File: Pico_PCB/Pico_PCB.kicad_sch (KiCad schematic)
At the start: 14 parts, among them J1 USB_A, J2 AVR-ISP-6, SW1 SPST_Momentary_4.6x2.8mm, U1 AT90USB647-A

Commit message: PCB_19/09
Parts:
- removed C1, C2, C4: C, symbol Device:C
- removed J2: AVR-ISP-6, symbol Connector:AVR-ISP-6
- removed L1: L, symbol Device:L
- added C10, C11: 100nF, Capacitor_SMD:C_0603_1608Metric_Pad1.08x0.95mm_HandSolder, symbol Device:C
- added C7, C8: 22 pF, Capacitor_SMD:C_0603_1608Metric_Pad1.08x0.95mm_HandSolder, symbol Device:C
- added C9: 4.7uF, Capacitor_SMD:C_0603_1608Metric_Pad1.08x0.95mm_HandSolder, symbol Device:C
- added D10, D11, D3, D4, D5, D6, D7, D8, D9: LED, LED_SMD:LED_0603_1608Metric_Pad1.05x0.95mm_HandSolder, symbol Device:LED
- added J4: Conn_02x04_Counter_Clockwise, Connector_IDC:IDC-Header_2x04_P2.54mm_Vertical, symbol Connector_Generic:Conn_02x04_Counter_Clockwise
- added R10, R11, R12, R13, R14, R5, R6, R8, R9: 1k, symbol Device:R
- added R4: 10k, symbol Device:R
- added R7: 1M, symbol Device:R
- added SW2: SPST_Momentary_4.6x2.8mm, SparkFun-Switch:Momentary_SMD_4.6x2.8mm, symbol SparkFun-Switch:SPST_Momentary_4.6x2.8mm
- added TP1, TP10, TP11, TP12, TP13, TP14, TP15, TP16, TP17, TP18, TP19, TP2, TP20, TP21, TP22, TP23, TP24, TP25, TP26, TP27, TP28, TP29, TP3, TP30, TP31, TP32, TP33, TP34, TP4, TP5, TP6, TP7, TP8, TP9: TestPoint, symbol Connector:TestPoint
- added Y1: Crystal_GND24, Crystal:Crystal_SMD_SeikoEpson_FA238-4Pin_3.2x2.5mm_HandSoldering, symbol Device:Crystal_GND24
- C3: value C -> 1uF
- R1, R2: value R -> 22
- R3: value R -> 10k
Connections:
- net 5V is gone; now on net +5V: J1.1 (VBUS), R3.1, U1.21 (VCC), U1.3 (UVCC), U1.52 (VCC), U1.64 (AVCC)
- net D+: now also R2.1; no longer R2.2
- net D-: now also R1.1; no longer R1.2
- net GND: now also D1.2 (A), D2.2 (A), C10.2, C11.2, C7.2, C8.2, C9.2, D10.1 (K), D11.1 (K), D3.1 (K), D4.1 (K), D5.1 (K), D6.1 (K), D7.1 (K), D8.1 (K), D9.1 (K), J4.1 (Pin_1), SW2.1 (A), Y1.2, Y1.4
- net MISO: now also J4.5 (Pin_5)
- net MOSI: now also J4.3 (Pin_3)
- net RESET: now also J4.6 (Pin_6)
- net SCK: now also J4.7 (Pin_7)
- net SS: now also J4.8 (Pin_8)
- net at D2.1 (K), J1.2 (D-): now also R1.2; no longer R1.1
- net at D1.1 (K), J1.3 (D+): now also R2.2; no longer R2.1
- net at U1.1 (PE6): now also TP27.1
- net INT: now reaches U1.14 (PB4)
- net INT: now also J4.4 (Pin_4)
- net at U1.15 (PB5): now also TP9.1
- net at U1.16 (PB6): now also TP10.1
- net at U1.17 (PB7): now also TP11.1
- net at U1.18 (PE4): now also TP25.1
- net at U1.19 (PE5): now also TP26.1
- net at U1.2 (PE7): now also TP28.1
- net at U1.23 (XTAL2): now also C8.1, R7.2, Y1.3
- net at U1.24 (XTAL1): now also C7.1, R7.1, Y1.1
- net at U1.25 (PD0): now also TP12.1
- net at U1.26 (PD1): now also TP13.1
- net at U1.27 (PD2): now also TP14.1
- net at U1.28 (PD3): now also TP15.1
- net at U1.29 (PD4): now also TP16.1
- net at U1.30 (PD5): now also TP17.1
- net at U1.31 (PD6): now also TP18.1
- net at U1.32 (PD7): now also TP19.1
- net at U1.33 (PE0): now also TP23.1
- net TEST0: now reaches U1.35 (PC0)
- net TEST0: now also R5.1
- net TEST1: now reaches U1.36 (PC1)
- net TEST1: now also R8.1
- net TEST2: now reaches U1.37 (PC2)
- net TEST2: now also R9.1
- net TEST3: now reaches U1.38 (PC3)
- net TEST3: now also R10.1
- net TEST4: now reaches U1.39 (PC4)
- net TEST4: now also R11.1
- net TEST5: now reaches U1.40 (PC5)
- net TEST5: now also R12.1
- net TEST6: now reaches U1.41 (PC6)
- net TEST6: now also R13.1
- net TEST7: now reaches U1.42 (PC7)
- net TEST7: now also R14.1
- net HWB: now reaches U1.43 (PE2/~{HWB})
- net HWB: now also R4.2, SW2.2 (B)
- net at U1.44 (PA7): now also TP8.1
- net at U1.45 (PA6): now also TP7.1
- net at U1.46 (PA5): now also TP6.1
- net at U1.47 (PA4): now also TP5.1
- net at U1.48 (PA3): now also TP4.1
- net at U1.49 (PA2): now also TP3.1
- net at U1.50 (PA1): now also TP2.1
- net at U1.51 (PA0): now also TP1.1
- net at U1.54 (PF7): now also TP20.1
- net at U1.55 (PF6): now also TP21.1
- net at U1.56 (PF5): now also TP34.1
- net at U1.57 (PF4): now also TP33.1
- net at U1.58 (PF3): now also TP32.1
- net at U1.59 (PF2): now also TP31.1
- net at U1.60 (PF1): now also TP30.1
- net at U1.61 (PF0): now also TP29.1
- net at U1.62 (AREF): now also TP22.1
- net +5V: now reaches U1.8 (VBUS)
- net +5V: now also C10.1, C11.1, C9.1, J4.2 (Pin_2), R4.1, R6.1
- net at U1.9 (PE3): now also TP24.1
- new net: D10.2 (A), R13.2
- new net: D11.2 (A), R14.2
- new net: D3.2 (A), R5.2
- new net: D8.2 (A), R11.2
- new net: D7.2 (A), R10.2
- new net: D4.2 (A), R8.2
- new net: D9.2 (A), R12.2
- new net: D5.2 (A), R6.2
- new net: D6.2 (A), R9.2
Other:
- note added: "Bouton HWB"
- note added: "Bouton de reset"
- note added: "Connection HE10"
- note added: "Découplage"
- note added: "LEDs de test"
- note added: "Port USB"
- moved on the sheet: C3, D1, D2, J1, R1, R2, R3, SW1, U1

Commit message: Routage_22_09
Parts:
- C3: footprint (none) -> Capacitor_SMD:C_0603_1608Metric_Pad1.08x0.95mm_HandSolder
- D1, D2: footprint (none) -> Diode_SMD:D_0603_1608Metric_Pad1.05x0.95mm_HandSolder
- J1: footprint SparkFun-Connector:USB-A-S-FEMALE_NoSilk -> Connectors:USB-A-S-NOSILK-FEMALE
- R1, R10, R11, R12, R13, R14, R2, R3, R4, R5, R6, R7, R8, R9: footprint (none) -> Resistor_SMD:R_0603_1608Metric_Pad0.98x0.95mm_HandSolder
- SW1, SW2: footprint SparkFun-Switch:Momentary_SMD_4.6x2.8mm -> Switches:TACTILE_SWITCH_SMD_5.2MM
- TP1, TP10, TP11, TP12, TP13, TP14, TP15, TP16, TP17, TP18, TP19, TP2, TP20, TP21, TP22, TP23, TP24, TP25, TP26, TP27, TP28, TP29, TP3, TP30, TP31, TP32, TP33, TP34, TP4, TP5, TP6, TP7, TP8, TP9: footprint (none) -> TestPoint:TestPoint_THTPad_D1.5mm_Drill0.7mm
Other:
- moved on the sheet: C10, C11, C9, D1, D10, D11, D2, D3, D4, D5, D6, D7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

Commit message: PCB_03/09
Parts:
- added C1: 1uF, Capacitor_SMD:C_0603_1608Metric_Pad1.08x0.95mm_HandSolder, symbol Device:C
- added TP35: TestPoint, TestPoint:TestPoint_THTPad_D1.5mm_Drill0.7mm, symbol Connector:TestPoint
- C10: value 100nF -> 1uF
- C9: value 4.7uF -> 100nF
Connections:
- net +5V: now also C1.1
- net GND: now also C1.2
- net at U1.34 (PE1): now also TP35.1
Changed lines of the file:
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@@
   (junction (at 118.11 160.02) (diameter 0) (color 0 0 0 0)
   )
+  (junction (at 160.02 33.02) (diameter 0) (color 0 0 0 0)
+  )
   (junction (at 96.52 77.47) (diameter 0) (color 0 0 0 0)
   )
+  (junction (at 165.1 40.64) (diameter 0) (color 0 0 0 0)
+  )
   (junction (at 96.52 69.85) (diameter 0) (color 0 0 0 0)
   )
+  (junction (at 165.1 33.02) (diameter 0) (color 0 0 0 0)
+  )
   (junction (at 99.06 99.06) (diameter 0) (color 0 0 0 0)
   )
@@
   (junction (at 76.2 69.85) (diameter 0) (color 0 0 0 0)
   )
+  (junction (at 160.02 40.64) (diameter 0) (color 0 0 0 0)
+  )
   (junction (at 76.2 82.55) (diameter 0) (color 0 0 0 0)
   )
@@
     (stroke (width 0) (type default))
   )
+  (wire (pts (xy 149.86 40.64) (xy 160.02 40.64))
+    (stroke (width 0) (type default))
+  )
   (wire (pts (xy 100.33 77.47) (xy 100.33 76.2))
     (stroke (width 0) (type default))
@@
     (stroke (width 0) (type default))
   )
+  (wire (pts (xy 149.86 33.02) (xy 160.02 33.02))
+    (stroke (width 0) (type default))
+  )
   (wire (pts (xy 76.2 69.85) (xy 96.52 69.85))
     (stroke (width 0) (type default))
@@
     (stroke (width 0) (type default))
   )
+  (wire (pts (xy 165.1 33.02) (xy 170.18 33.02))
+    (stroke (width 0) (type default))
+  )
   (wire (pts (xy 59.69 77.47) (xy 62.23 77.47))
     (stroke (width 0) (type default))
@@
     (stroke (width 0) (type default))
   )
-  (wire (pts (xy 160.02 40.64) (xy 170.18 40.64))
+  (wire (pts (xy 160.02 40.64) (xy 165.1 40.64))
     (stroke (width 0) (type default))
   )
@@
     (stroke (width 0) (type default))
   )
+  (wire (pts (xy 44.45 162.56) (xy 45.72 162.56))
+    (stroke (width 0) (type default))
+  )
   (wire (pts (xy 93.98 106.68) (xy 99.06 106.68))
     (stroke (width 0) (type default))
@@
     (stroke (width 0) (type default))
   )
+  (wire (pts (xy 165.1 40.64) (xy 170.18 40.64))
+    (stroke (width 0) (type default))
+  )
   (wire (pts (xy 184.15 143.51) (xy 184.15 144.78))
     (stroke (width 0) (type default))
@@
     (stroke (width 0) (type default))
   )
-  (wire (pts (xy 170.18 30.48) (xy 170.18 33.02))
+  (wire (pts (xy 165.1 30.48) (xy 165.1 33.02))
+    (stroke (width 0) (type default))
+  )
+  (wire (pts (xy 165.1 40.64) (xy 165.1 43.18))
+    (stroke (width 0) (type default))
+  )
+  (wire (pts (xy 209.55 143.51) (xy 209.55 144.78))
+    (stroke (width 0) (type default))
+  )
+  (wire (pts (xy 99.06 99.06) (xy 102.87 99.06))
+    (stroke (width 0) (type default))
+  )
+  (wire (pts (xy 81.28 82.55) (xy 81.28 73.66))
+    (stroke (width 0) (type default))
+  )
+  (wire (pts (xy 170.18 40.64) (xy 181.61 40.64))
+    (stroke (width 0) (type default))
+  )
+  (wire (pts (xy 100.33 69.85) (xy 100.33 71.12))
+    (stroke (width 0) (type default))
+  )
+  (wire (pts (xy 35.56 172.72) (xy 36.83 172.72))
+    (stroke (width 0) (type default))
+  )
+  (wire (pts (xy 227.33 143.51) (xy 227.33 144.78))
     (stroke (width 0) (type default))
   )
@@
     (stroke (width 0) (type default))
   )
-  (wire (pts (xy 170.18 40.64) (xy 170.18 43.18))
-    (stroke (width 0) (type default))
-  )
-  (wire (pts (xy 209.55 143.51) (xy 209.55 144.78))
-    (stroke (width 0) (type default))
-  )
-  (wire (pts (xy 99.06 99.06) (xy 102.87 99.06))
-    (stroke (width 0) (type default))
-  )
-  (wire (pts (xy 81.28 82.55) (xy 81.28 73.66))
-    (stroke (width 0) (type default))
-  )
-  (wire (pts (xy 170.18 40.64) (xy 181.61 40.64))
-    (stroke (width 0) (type default))
-  )
-  (wire (pts (xy 100.33 69.85) (xy 100.33 71.12))
-    (stroke (width 0) (type default))
-  )
-  (wire (pts (xy 35.56 172.72) (xy 36.83 172.72))
-    (stroke (width 0) (type default))
-  )
-  (wire (pts (xy 227.33 143.51) (xy 227.33 144.78))
-    (stroke (width 0) (type default))
-  )
   (wire (pts (xy 168.91 97.79) (xy 157.48 97.79))
     (stroke (width 0) (type default))
   )
-  (wire (pts (xy 160.02 33.02) (xy 170.18 33.02))
+  (wire (pts (xy 160.02 33.02) (xy 165.1 33.02))
     (stroke (width 0) (type default))
   )
@@
     (stroke (width 0) (type default))
   )
-  (wire (pts (xy 44.45 162.56) (xy 45.72 162.56))
-    (stroke (width 0) (type default))
-  )
   (wire (pts (xy 59.69 162.56) (xy 58.42 162.56))
     (stroke (width 0) (type default))
@@
     (fill (type none))
   )
-  (rectangle (start 149.86 19.05) (end 194.31 54.61)
+  (rectangle (start 140.97 19.05) (end 194.31 54.61)
     (stroke (width 0) (type default))
     (fill (type none))
@@
     )
   )
-  (symbol (lib_id "power:GND") (at 170.18 43.18 0) (unit 1)
-    (in_bom yes) (on_board yes) (dnp no) (fields_autoplaced)
-    (property "Reference" "#PWR015" (at 170.18 49.53 0)
-      (effects (font (size 1.27 1.27)) hide)
-    )
-    (property "Value" "GND" (at 170.18 48.26 0)
-      (effects (font (size 1.27 1.27)))
-    )
-    (property "Footprint" "" (at 170.18 43.18 0)
-      (effects (font (size 1.27 1.27)) hide)
-    )
-    (property "Datasheet" "" (at 170.18 43.18 0)
+  (symbol (lib_id "power:GND") (at 165.1 43.18 0) (unit 1)
+    (in_bom yes) (on_board yes) (dnp no) (fields_autoplaced)
+    (property "Reference" "#PWR015" (at 165.1 49.53 0)
+      (effects (font (size 1.27 1.27)) hide)
+    )
+    (property "Value" "GND" (at 165.1 48.26 0)
+      (effects (font (size 1.27 1.27)))
+    )
+    (property "Footprint" "" (at 165.1 43.18 0)
+      (effects (font (size 1.27 1.27)) hide)
+    )
+    (property "Datasheet" "" (at 165.1 43.18 0)
       (effects (font (size 1.27 1.27)) hide)
     )
@@
     )
   )
+  (symbol (lib_id "Device:C") (at 149.86 36.83 0) (unit 1)
+    (in_bom yes) (on_board yes) (dnp no) (fields_autoplaced)
+    (property "Reference" "C1" (at 153.67 35.56 0)
+      (effects (font (size 1.27 1.27)) (justify left))
+    )
+    (property "Value" "1uF" (at 153.67 38.1 0)
+      (effects (font (size 1.27 1.27)) (justify left))
+    )
+    (property "Footprint" "Capacitor_SMD:C_0603_1608Metric_Pad1.08x0.95mm_HandSolder" (at 150.8252 40.64 0)
+      (effects (font (size 1.27 1.27)) hide)
+    )
+    (property "Datasheet" "~" (at 149.86 36.83 0)
+      (effects (font (size 1.27 1.27)) hide)
+    )
+    (pin "1")
+    (pin "2")
+    (instances
+      (project "Pico_PCB"
+        (path "/080ce183-1edb-4a51-b877-ef257db80548"
+          (reference "C1") (unit 1)
+        )
+      )
+    )
+  )
   (symbol (lib_id "Device:R") (at 55.88 118.11 0) (unit 1)
     (in_bom yes) (on_board yes) (dnp no) (fields_autoplaced)
@@
       (effects (font (size 1.27 1.27)) (justify left))
     )
-    (property "Value" "100nF" (at 173.99 38.1 0)
+    (property "Value" "1uF" (at 173.99 38.1 0)
       (effects (font (size 1.27 1.27)) (justify left))
     )
@@
       (effects (font (size 1.27 1.27)) (justify left))
     )
-    (property "Value" "4.7uF" (at 163.83 38.1 0)
+    (property "Value" "100nF" (at 163.83 38.1 0)
       (effects (font (size 1.27 1.27)) (justify left))
     )
@@
     )
   )
+  (symbol (lib_id "Connector:TestPoint") (at 102.87 114.3 90) (unit 1)
+    (in_bom yes) (on_board yes) (dnp no) (fields_autoplaced)
+    (property "Reference" "TP35" (at 97.79 115.57 90)
+      (effects (font (size 1.27 1.27)) (justify left) hide)
+    )
+    (property "Value" "TestPoint" (at 97.79 113.03 90)
+      (effects (font (size 1.27 1.27)) (justify left) hide)
+    )
+    (property "Footprint" "TestPoint:TestPoint_THTPad_D1.5mm_Drill0.7mm" (at 102.87 109.22 0)
+      (effects (font (size 1.27 1.27)) hide)
+    )
+    (property "Datasheet" "~" (at 102.87 109.22 0)
+      (effects (font (size 1.27 1.27)) hide)
+    )
+    (pin "1")
+    (instances
+      (project "Pico_PCB"
+        (path "/080ce183-1edb-4a51-b877-ef257db80548"
+          (reference "TP35") (unit 1)
+        )
+      )
+    )
+  )
   (symbol (lib_id "Device:R") (at 184.15 132.08 0) (unit 1)
     (in_bom yes) (on_board yes) (dnp no) (fields_autoplaced)
@@
     )
   )
-  (symbol (lib_id "power:+5V") (at 170.18 30.48 0) (unit 1)
-    (in_bom yes) (on_board yes) (dnp no) (fields_autoplaced)
-    (property "Reference" "#PWR026" (at 170.18 34.29 0)
-      (effects (font (size 1.27 1.27)) hide)
-    )
-    (property "Value" "+5V" (at 170.18 25.4 0)
-      (effects (font (size 1.27 1.27)))
-    )
-    (property "Footprint" "" (at 170.18 30.48 0)
-      (effects (font (size 1.27 1.27)) hide)
-    )
-    (property "Datasheet" "" (at 170.18 30.48 0)
-      (effects (font (size 1.27 1.27)) hide)
-    )
+  (symbol (lib_id "power:+5V") (at 165.1 30.48 0) (unit 1)
+    (in_bom yes) (on_board yes) (dnp no) (fields_autoplaced)
+    (property "Reference" "#PWR026" (at 165.1 34.29 0)
+      (effects (font (size 1.27 1.27)) hide)
+    )
+    (property "Value" "+5V" (at 165.1 25.4 0)
+      (effects (font (size 1.27 1.27)))
+    )
+    (property "Footprint" "" (at 165.1 30.48 0)
+      (effects (font (size 1.27 1.27)) hide)
+    )
+    (property "Datasheet" "" (at 165.1 30.48 0)
+      (effects (font (size 1.27 1.27)) hide)
+    )

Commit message: PCB_fini
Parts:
- removed TP12: TestPoint, TestPoint:TestPoint_THTPad_D1.5mm_Drill0.7mm, symbol Connector:TestPoint
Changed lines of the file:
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@@
-    )
-  )
-  (symbol (lib_id "Connector:TestPoint") (at 133.35 134.62 270) (unit 1)
-    (in_bom yes) (on_board yes) (dnp no) (fields_autoplaced)
-    (property "Reference" "TP12" (at 138.43 133.35 90)
-      (effects (font (size 1.27 1.27)) (justify left) hide)
-    )
-    (property "Value" "TestPoint" (at 138.43 135.89 90)
-      (effects (font (size 1.27 1.27)) (justify left) hide)
-    )
-    (property "Footprint" "TestPoint:TestPoint_THTPad_D1.5mm_Drill0.7mm" (at 133.35 139.7 0)
-      (effects (font (size 1.27 1.27)) hide)
-    )
-    (property "Datasheet" "~" (at 133.35 139.7 0)
-      (effects (font (size 1.27 1.27)) hide)
-    )
-    (pin "1")
-    (instances
-      (project "Pico_PCB"
-        (path "/080ce183-1edb-4a51-b877-ef257db80548"
-          (reference "TP12") (unit 1)
-        )
-      )
     )
   )

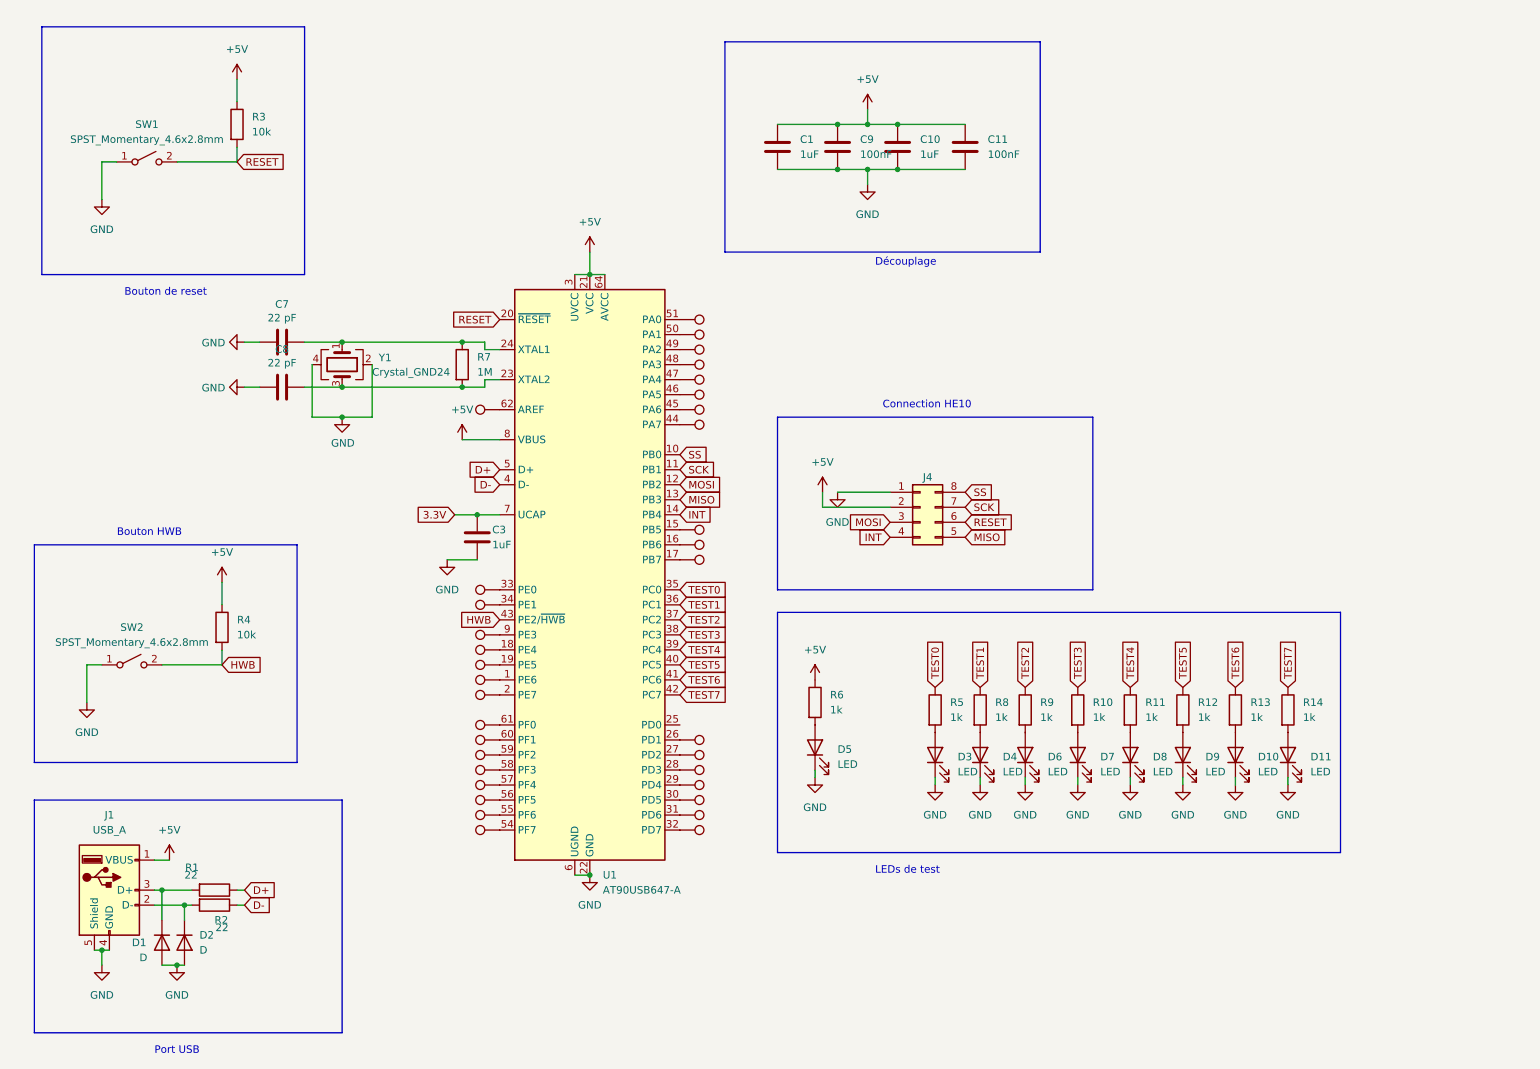
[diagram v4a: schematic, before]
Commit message: Modif PCB boutons
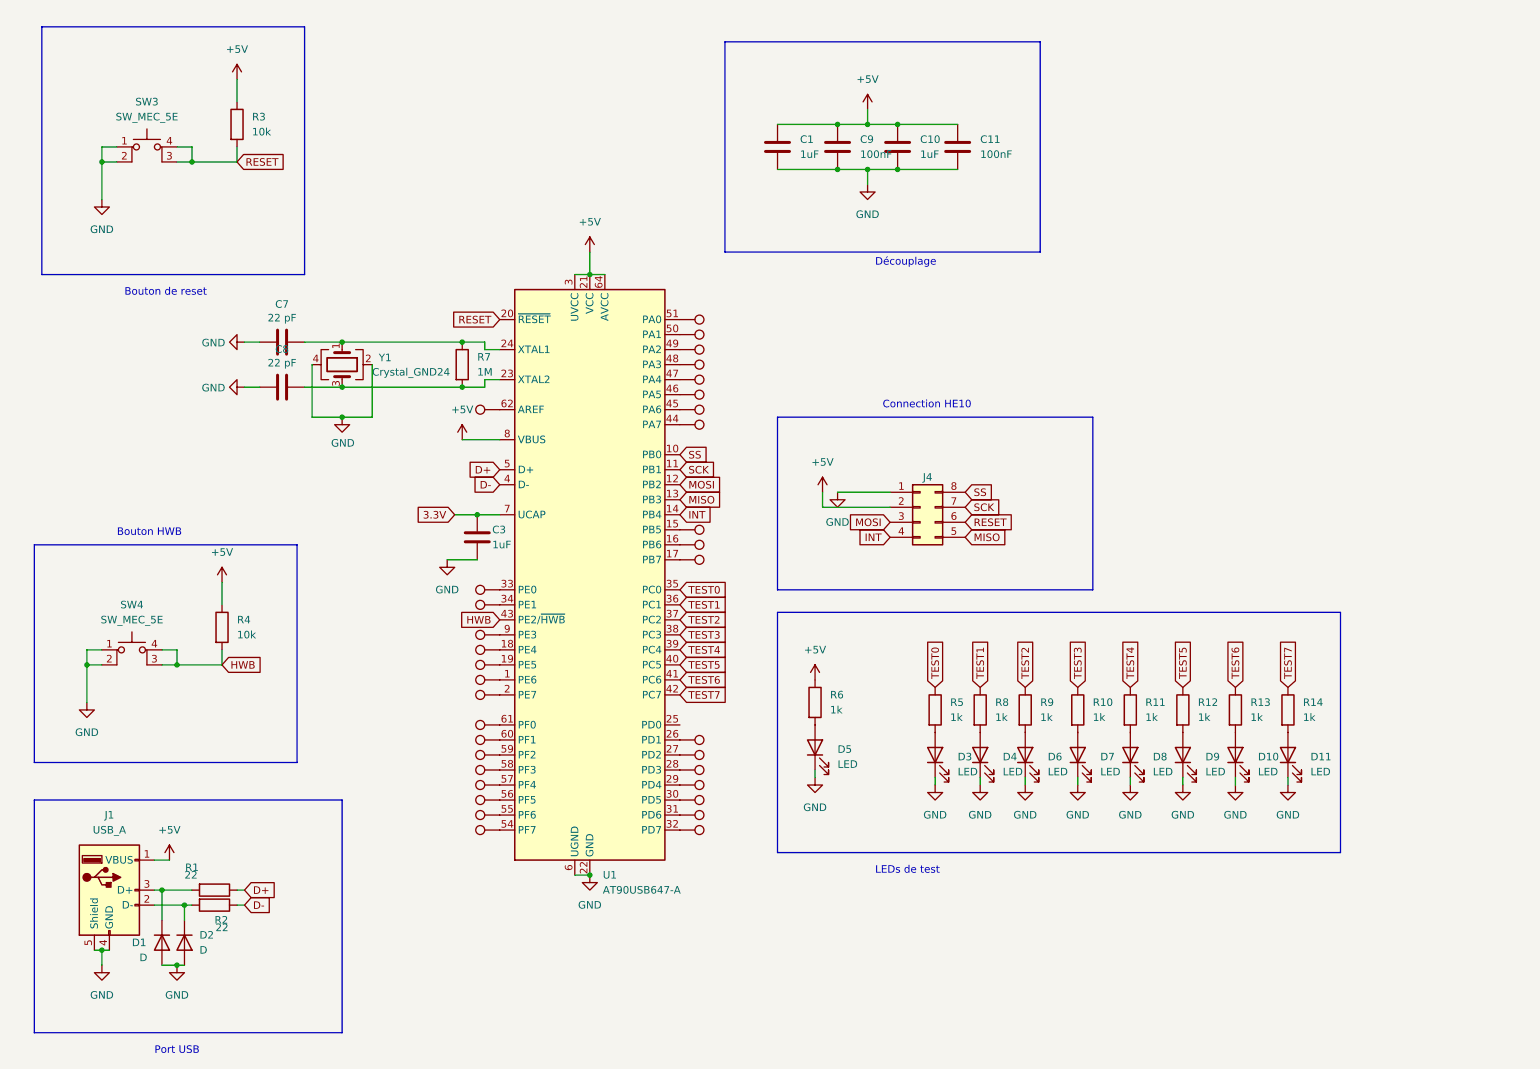
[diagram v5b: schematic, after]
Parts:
- removed SW1, SW2: SPST_Momentary_4.6x2.8mm, Switches:TACTILE_SWITCH_SMD_5.2MM, symbol SparkFun-Switch:SPST_Momentary_4.6x2.8mm
- added SW3, SW4: SW_MEC_5E, Spark-Switches:TACTILE_SWITCH_SMD_5.2MM, symbol Switch:SW_MEC_5E
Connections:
- net GND: now also SW3.1, SW3.2, SW4.1, SW4.2
- net HWB: now also SW4.3 (K), SW4.4 (A)
- net RESET: now also SW3.3 (K), SW3.4 (A)
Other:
- moved on the sheet: C11
